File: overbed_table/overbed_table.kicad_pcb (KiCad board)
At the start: 2 copper layers, 10 parts, among them U1 TPS562201DDCR, U2 TPS562201DDCR, U3 TM1638

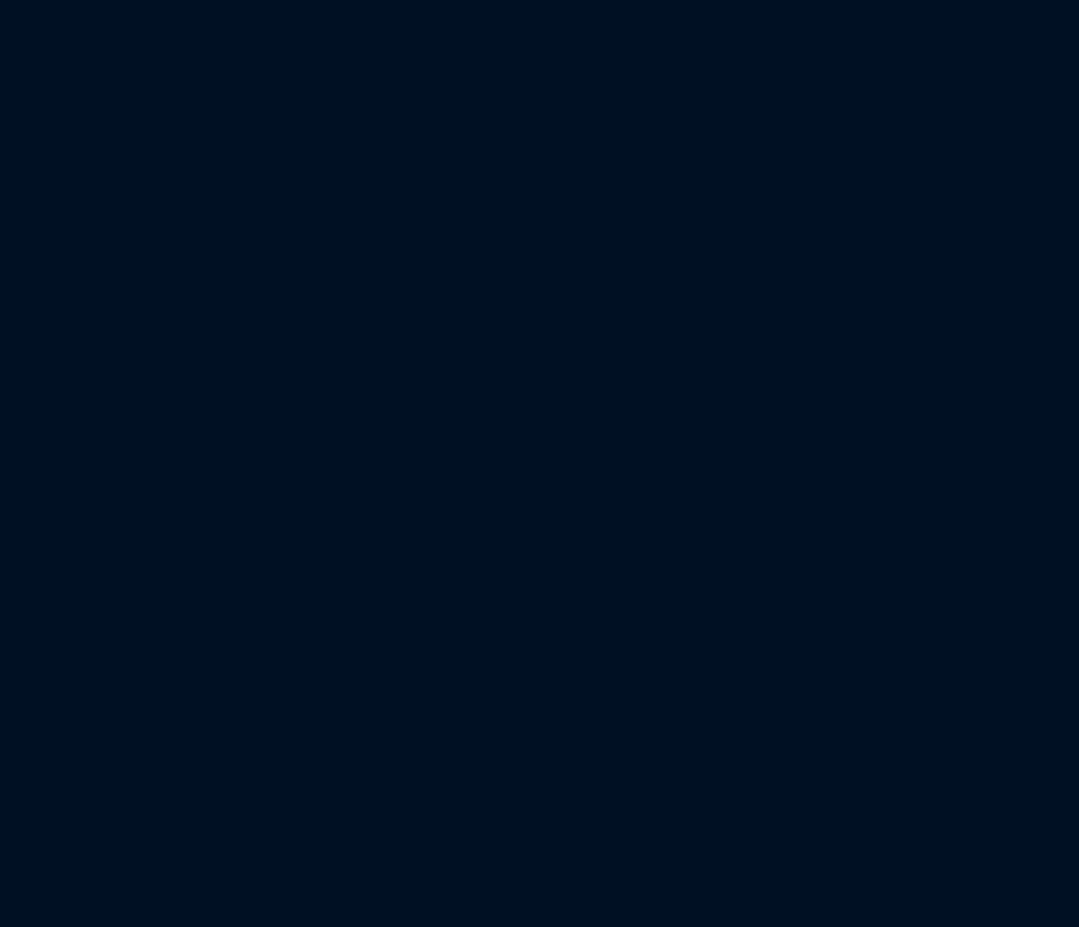
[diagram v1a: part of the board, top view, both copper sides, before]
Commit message: 更新步进驱动等
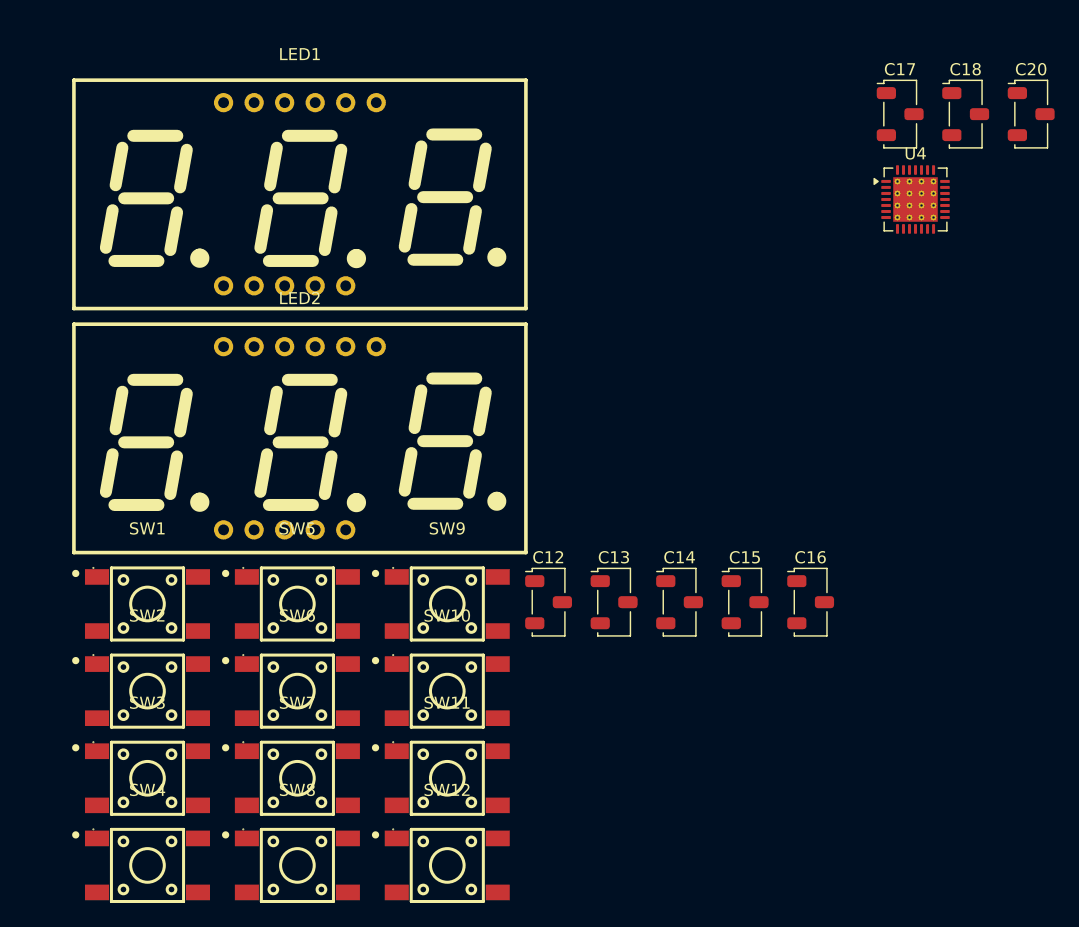
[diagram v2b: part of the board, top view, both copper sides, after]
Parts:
- added C12: 0.1uF, Button_Switch_SMD:Nidec_Copal_CAS-120A, F.Cu at (248.6, 111.6)
- added C13: 100uF, Button_Switch_SMD:Nidec_Copal_CAS-120A, F.Cu at (254.1, 111.6)
- added C14: 100pF, Button_Switch_SMD:Nidec_Copal_CAS-120A, F.Cu at (259.5, 111.6)
- added C15: 100pF, Button_Switch_SMD:Nidec_Copal_CAS-120A, F.Cu at (265.0, 111.6)
- added C16: 100pF, Button_Switch_SMD:Nidec_Copal_CAS-120A, F.Cu at (270.4, 111.6)
- added C17: 22nF, Button_Switch_SMD:Nidec_Copal_CAS-120A, F.Cu at (277.9, 71.0)
- added C18: 100nF, Button_Switch_SMD:Nidec_Copal_CAS-120A, F.Cu at (283.3, 71.0)
- added C20: 100nF, Button_Switch_SMD:Nidec_Copal_CAS-120A, F.Cu at (288.8, 71.0)
- added LED1: FJ5361BW, lcsc_footprints:C2938342_LED-SEG-TH_11P-L37_5-W19_0-P2_54-LS15_2-BL, F.Cu at (227.9, 77.6)
- added LED2: FJ5361BW, lcsc_footprints:C2938342_LED-SEG-TH_11P-L37_5-W19_0-P2_54-LS15_2-BL, F.Cu at (227.9, 97.9)
- added SW1: KH-6X6X6H-STM, lcsc_footprints:C2837532_SW-SMD_4P-L6_0-W6_0-P4_50-LS9_0_KH-6X6X6H-STM, F.Cu at (215.3, 111.7)
- added SW10: KH-6X6X6H-STM, lcsc_footprints:C2837532_SW-SMD_4P-L6_0-W6_0-P4_50-LS9_0_KH-6X6X6H-STM, F.Cu at (240.2, 119.0)
- added SW11: KH-6X6X6H-STM, lcsc_footprints:C2837532_SW-SMD_4P-L6_0-W6_0-P4_50-LS9_0_KH-6X6X6H-STM, F.Cu at (240.2, 126.2)
- added SW12: KH-6X6X6H-STM, lcsc_footprints:C2837532_SW-SMD_4P-L6_0-W6_0-P4_50-LS9_0_KH-6X6X6H-STM, F.Cu at (240.2, 133.5)
- added SW2: KH-6X6X6H-STM, lcsc_footprints:C2837532_SW-SMD_4P-L6_0-W6_0-P4_50-LS9_0_KH-6X6X6H-STM, F.Cu at (215.3, 119.0)
- added SW3: KH-6X6X6H-STM, lcsc_footprints:C2837532_SW-SMD_4P-L6_0-W6_0-P4_50-LS9_0_KH-6X6X6H-STM, F.Cu at (215.3, 126.2)
- added SW4: KH-6X6X6H-STM, lcsc_footprints:C2837532_SW-SMD_4P-L6_0-W6_0-P4_50-LS9_0_KH-6X6X6H-STM, F.Cu at (215.3, 133.5)
- added SW5: KH-6X6X6H-STM, lcsc_footprints:C2837532_SW-SMD_4P-L6_0-W6_0-P4_50-LS9_0_KH-6X6X6H-STM, F.Cu at (227.7, 111.7)
- added SW6: KH-6X6X6H-STM, lcsc_footprints:C2837532_SW-SMD_4P-L6_0-W6_0-P4_50-LS9_0_KH-6X6X6H-STM, F.Cu at (227.7, 119.0)
- added SW7: KH-6X6X6H-STM, lcsc_footprints:C2837532_SW-SMD_4P-L6_0-W6_0-P4_50-LS9_0_KH-6X6X6H-STM, F.Cu at (227.7, 126.2)
- added SW8: KH-6X6X6H-STM, lcsc_footprints:C2837532_SW-SMD_4P-L6_0-W6_0-P4_50-LS9_0_KH-6X6X6H-STM, F.Cu at (227.7, 133.5)
- added SW9: KH-6X6X6H-STM, lcsc_footprints:C2837532_SW-SMD_4P-L6_0-W6_0-P4_50-LS9_0_KH-6X6X6H-STM, F.Cu at (240.2, 111.7)
- added U4: TMC2209-LA, Package_DFN_QFN:VQFN-28-1EP_5x5mm_P0.5mm_EP3.7x3.7mm_ThermalVias, F.Cu at (279.2, 78.1)
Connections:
- U3 pad 10: unconnected-(U3-SEG6/K6-Pad10) -> /数码管_按钮/SEG6
- U3 pad 11: unconnected-(U3-SEG7/K7-Pad11) -> /数码管_按钮/SEG7
- U3 pad 12: unconnected-(U3-SEG8/K8-Pad12) -> /数码管_按钮/SEG8
- U3 pad 15: unconnected-(U3-VDD-Pad15) -> +5V
- U3 pad 18: unconnected-(U3-GND-Pad18) -> GND
- U3 pad 19: unconnected-(U3-GR6-Pad19) -> /数码管_按钮/GRID6
- U3 pad 2: unconnected-(U3-K2-Pad2) -> Net-(SW5-A)
- U3 pad 20: unconnected-(U3-GR5-Pad20) -> /数码管_按钮/GRID5
- U3 pad 21: unconnected-(U3-GR4-Pad21) -> /数码管_按钮/GRID4
- U3 pad 22: unconnected-(U3-GR3-Pad22) -> /数码管_按钮/GRID3
- U3 pad 23: unconnected-(U3-GR2-Pad23) -> /数码管_按钮/GRID2
- U3 pad 24: unconnected-(U3-GR1-Pad24) -> /数码管_按钮/GRID1
- U3 pad 25: unconnected-(U3-GND-Pad25) -> GND
- U3 pad 26: unconnected-(U3-DIO-Pad26) -> /数码管_按钮/DIO
- U3 pad 27: unconnected-(U3-CLK-Pad27) -> /数码管_按钮/CLK
- U3 pad 28: unconnected-(U3-STB-Pad28) -> /数码管_按钮/STB
- U3 pad 3: unconnected-(U3-K3-Pad3) -> Net-(SW1-A)
- U3 pad 4: unconnected-(U3-VDD-Pad4) -> +5V
- U3 pad 5: unconnected-(U3-SEG1/K1-Pad5) -> /数码管_按钮/SEG1
- U3 pad 6: unconnected-(U3-SEG2/K2-Pad6) -> /数码管_按钮/SEG2
- U3 pad 7: unconnected-(U3-SEG3/K3-Pad7) -> /数码管_按钮/SEG3
- U3 pad 8: unconnected-(U3-SEG4/K4-Pad8) -> /数码管_按钮/SEG4
- U3 pad 9: unconnected-(U3-SEG5/K5-Pad9) -> /数码管_按钮/SEG5

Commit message: 更新原理图
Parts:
- added C1: 10uF, Capacitor_SMD:C_0603_1608Metric, F.Cu at (78.6, 144.2)
- added C21: C, Display_7Segment:HDSP-7401, F.Cu at (46.5, 118.7)
- added C22: 100nF, Display_7Segment:HDSP-7401, F.Cu at (55.8, 118.7)
- added C23: 100nF, Display_7Segment:HDSP-7401, F.Cu at (65.1, 118.7)
- added C24: 100uF, Display_7Segment:HDSP-7401, F.Cu at (74.4, 118.7)
- added C25: 100nF, lcsc_footprints:C5342036_HVSSOP-28_L7_1-W3_0-P0_50-LS4_9-BL-EP, F.Cu at (33.8, 108.9)
- added C26: 220uF, lcsc_footprints:C5342036_HVSSOP-28_L7_1-W3_0-P0_50-LS4_9-BL-EP, F.Cu at (26.2, 119.1)
- added C27: 10nF, lcsc_footprints:C5342036_HVSSOP-28_L7_1-W3_0-P0_50-LS4_9-BL-EP, F.Cu at (24.8, 132.4)
- added C28: 100nF, lcsc_footprints:C5342036_HVSSOP-28_L7_1-W3_0-P0_50-LS4_9-BL-EP, F.Cu at (38.2, 134.1)
- added C29: 100nF, lcsc_footprints:C5342036_HVSSOP-28_L7_1-W3_0-P0_50-LS4_9-BL-EP, F.Cu at (21.2, 150.1)
- added C30: 100nF, lcsc_footprints:C5342036_HVSSOP-28_L7_1-W3_0-P0_50-LS4_9-BL-EP, F.Cu at (18.8, 167.1)
- added C31: 10uF, Capacitor_SMD:C_0603_1608Metric, F.Cu at (58.2, 147.3)
- added C31: 10uF, lcsc_footprints:C19188399_SOT-563-6_L1_6-W1_2-P0_50-LS1_6-BL, F.Cu at (57.8, 144.4)
- added C32: 10uF, Capacitor_SMD:C_0603_1608Metric, F.Cu at (58.2, 149.8)
- added C32: 10uF, lcsc_footprints:C19188399_SOT-563-6_L1_6-W1_2-P0_50-LS1_6-BL, F.Cu at (60.9, 144.4)
- added C33: 100nF, lcsc_footprints:C19188399_SOT-563-6_L1_6-W1_2-P0_50-LS1_6-BL, F.Cu at (64.0, 144.4)
- added C34: 22uF, lcsc_footprints:C19188399_SOT-563-6_L1_6-W1_2-P0_50-LS1_6-BL, F.Cu at (67.0, 144.4)
- added C35: 22uF, lcsc_footprints:C19188399_SOT-563-6_L1_6-W1_2-P0_50-LS1_6-BL, F.Cu at (70.1, 144.4)
- added C36: 22uF, lcsc_footprints:C19188399_SOT-563-6_L1_6-W1_2-P0_50-LS1_6-BL, F.Cu at (73.1, 144.4)
- added C4: 10uF, Capacitor_SMD:C_0603_1608Metric, F.Cu at (78.6, 146.7)
- added D1: 1N4148W, PCM_Diode_SMD_AKL:D_SOD-123, F.Cu at (47.3, 145.0)
- added D2: 1N4148W, PCM_Diode_SMD_AKL:D_SOD-123, F.Cu at (47.3, 149.1)
- added D3: 1N4148W, PCM_Diode_SMD_AKL:D_SOD-123, F.Cu at (47.3, 153.2)
- added D4: 1N4148W, PCM_Diode_SMD_AKL:D_SOD-123, F.Cu at (47.3, 157.3)
- added D5: 1N4148W, PCM_Diode_SMD_AKL:D_SOD-123, F.Cu at (47.3, 161.4)
- added D6: 1N4148W, PCM_Diode_SMD_AKL:D_SOD-123, F.Cu at (47.3, 165.5)
- added Q1: BSS138, PCM_Package_TO_SOT_SMD_AKL:SOT-23, F.Cu at (62.6, 160.4)
- added R10: 1k, PCM_SparkFun-Resistor:R_0603_1608Metric, F.Cu at (46.3, 132.2)
- added R11: 10k, PCM_SparkFun-Resistor:R_0603_1608Metric, F.Cu at (46.3, 134.7)
- added R12: 0.15, PCM_SparkFun-Resistor:R_0603_1608Metric, F.Cu at (46.3, 137.2)
- added R13: 0.15, PCM_SparkFun-Resistor:R_0603_1608Metric, F.Cu at (46.3, 139.7)
- added R14: 10k, PCM_SparkFun-Resistor:R_0603_1608Metric, F.Cu at (40.3, 117.8)
- added R15: 10k, PCM_SparkFun-Resistor:R_0603_1608Metric, F.Cu at (40.3, 120.3)
- added R16: 1k, PCM_SparkFun-Resistor:R_0603_1608Metric, F.Cu at (40.3, 122.8)
- added R17: 4.7k, PCM_SparkFun-Resistor:R_0603_1608Metric, F.Cu at (40.3, 125.3)
- added R18: 33.2k, PCM_SparkFun-Resistor:R_0603_1608Metric, F.Cu at (58.2, 152.3)
- added R19: 10k, PCM_SparkFun-Resistor:R_0603_1608Metric, F.Cu at (58.2, 154.8)
- added R3: 33.2k, PCM_SparkFun-Resistor:R_0603_1608Metric, F.Cu at (78.6, 149.2)
- added R4: 10k, PCM_SparkFun-Resistor:R_0603_1608Metric, F.Cu at (78.6, 151.7)
- added R5: 10k, PCM_SparkFun-Resistor:R_0603_1608Metric, F.Cu at (52.2, 144.2)
- added R6: 10k, PCM_SparkFun-Resistor:R_0603_1608Metric, F.Cu at (52.2, 146.7)
- added R7: 10k, PCM_SparkFun-Resistor:R_0603_1608Metric, F.Cu at (52.2, 149.2)
- added R8: 4.7k, PCM_SparkFun-Resistor:R_0603_1608Metric, F.Cu at (58.2, 159.3)
- added R9: 4.7k, PCM_SparkFun-Resistor:R_0603_1608Metric, F.Cu at (58.2, 161.8)
- added U5: DRV8243SQDGQRQ1, lcsc_footprints:C5342036_HVSSOP-28_L7_1-W3_0-P0_50-LS4_9-BL-EP, F.Cu at (36.8, 167.6)
- added U6: TPS562201DDCR, lcsc_footprints:C90061_SOT-23-6_L2_9-W1_6-P0_95-LS2_8-BR, F.Cu at (127.5, 139.0)

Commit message: 原理图V1.0
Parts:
- removed the C1 at (78.6, 144.2)
- removed the C1 at (103.1, 90.3)
- removed the C31 at (58.2, 147.3)
- removed the C31 at (57.8, 144.4)
- removed the C32 at (58.2, 149.8)
- removed the C32 at (60.9, 144.4)
- removed the C4 at (112.3, 90.3)
- removed the C4 at (78.6, 146.7)
- added C1: 1uF, Capacitor_SMD:C_0603_1608Metric, F.Cu at (93.5, 53.8)
- added C10: 100nF, Capacitor_SMD:C_0805_2012Metric, F.Cu at (166.3, 153.3)
- added C11: 22uF, Capacitor_SMD:C_0805_2012Metric, F.Cu at (166.3, 156.3)
- added C19: 100pF, Capacitor_SMD:C_0603_1608Metric, F.Cu at (98.4, 102.9)
- added C31: 100nF, Capacitor_SMD:C_0603_1608Metric, F.Cu at (173.9, 72.9)
- added C32: 4.7uF, Capacitor_SMD:C_0603_1608Metric, F.Cu at (173.9, 75.4)
- added C37: 4.7uF, Capacitor_SMD:C_0603_1608Metric, F.Cu at (181.9, 164.1)
- added C38: 10uF, Capacitor_SMD:C_0805_2012Metric, F.Cu at (128.4, 155.8)
- added C38: 10uF, Capacitor_SMD:C_0603_1608Metric, F.Cu at (132.6, 155.5)
- added C39: 10uF, Capacitor_SMD:C_0603_1608Metric, F.Cu at (132.6, 158.0)
- added C39: 10uF, Capacitor_SMD:C_0805_2012Metric, F.Cu at (128.4, 158.8)
- added C4: 1uF, Capacitor_SMD:C_0603_1608Metric, F.Cu at (93.5, 58.9)
- added C40: 100nF, Capacitor_SMD:C_0805_2012Metric, F.Cu at (128.4, 161.8)
- added C41: 22uF, Capacitor_SMD:C_0805_2012Metric, F.Cu at (128.4, 164.8)
- added C42: 22uF, Capacitor_SMD:C_0805_2012Metric, F.Cu at (128.4, 167.8)
- added C43: 22uF, Capacitor_SMD:C_0805_2012Metric, F.Cu at (128.4, 170.8)
- added C44: 1uF, Capacitor_SMD:C_0603_1608Metric, F.Cu at (147.5, 124.6)
- added C45: 1uF, Capacitor_SMD:C_0603_1608Metric, F.Cu at (147.5, 127.1)
- added C46: 100nF, Capacitor_SMD:C_0603_1608Metric, F.Cu at (147.5, 129.6)
- added C47: 1uF, Capacitor_SMD:C_0603_1608Metric, F.Cu at (147.5, 132.1)
- added C48: 1uF, Capacitor_SMD:C_0603_1608Metric, F.Cu at (147.5, 134.6)
- added C49: 1nF, Capacitor_SMD:C_0603_1608Metric, F.Cu at (151.5, 124.6)
- added C50: 1uF, Capacitor_SMD:C_0603_1608Metric, F.Cu at (151.5, 127.1)
- added C51: 1nF, Capacitor_SMD:C_0603_1608Metric, F.Cu at (151.5, 129.6)
- added C52: 1uF, Capacitor_SMD:C_0603_1608Metric, F.Cu at (155.3, 59.9)
- added C53: 1uF, Capacitor_SMD:C_0603_1608Metric, F.Cu at (155.3, 62.4)
- added C54: 100nF, Capacitor_SMD:C_0603_1608Metric, F.Cu at (155.3, 64.9)
- added C55: 1uF, Capacitor_SMD:C_0603_1608Metric, F.Cu at (155.3, 67.4)
- added C56: 1uF, Capacitor_SMD:C_0603_1608Metric, F.Cu at (155.3, 69.9)
- added C57: 1nF, Capacitor_SMD:C_0603_1608Metric, F.Cu at (159.3, 59.9)
- added C58: 1uF, Capacitor_SMD:C_0603_1608Metric, F.Cu at (159.3, 62.4)
- added C59: 1nF, Capacitor_SMD:C_0603_1608Metric, F.Cu at (159.3, 64.9)
- added C60: 100nF, Capacitor_SMD:C_0603_1608Metric, F.Cu at (173.9, 38.3)
- added C61: 100nF, Capacitor_SMD:C_0603_1608Metric, F.Cu at (173.9, 40.8)
- added C62: 100nF, Capacitor_SMD:C_0603_1608Metric, F.Cu at (173.9, 43.3)
- added C63: 100uF, Capacitor_SMD:CP_Elec_6.3x7.7, F.Cu at (181.1, 41.1)
- added C64: 100nF, Capacitor_SMD:C_0603_1608Metric, F.Cu at (173.9, 45.8)
- added C65: 100nF, Capacitor_SMD:C_0603_1608Metric, F.Cu at (173.9, 48.3)
- added C66: 4.7uF, Capacitor_SMD:C_0603_1608Metric, F.Cu at (173.9, 50.8)
- added C67: 22nF, Capacitor_SMD:C_0603_1608Metric, F.Cu at (173.9, 53.3)
- added C68: 100nF, Capacitor_SMD:C_0603_1608Metric, F.Cu at (181.9, 147.0)
- added C69: 4.7uF, Capacitor_SMD:C_0603_1608Metric, F.Cu at (181.9, 149.5)
- added C7: 1uF, Capacitor_SMD:C_0603_1608Metric, F.Cu at (97.5, 56.3)
- added C70: 10uF, Capacitor_SMD:C_0603_1608Metric, F.Cu at (116.8, 155.5)
- added C70: 10uF, Capacitor_SMD:C_0805_2012Metric, F.Cu at (112.5, 155.8)
- added C71: 10uF, Capacitor_SMD:C_0603_1608Metric, F.Cu at (116.8, 158.0)
- added C71: 10uF, Capacitor_SMD:C_0805_2012Metric, F.Cu at (112.5, 158.8)
- added C72: 100nF, Capacitor_SMD:C_0805_2012Metric, F.Cu at (112.5, 161.8)
- added C73: 22uF, Capacitor_SMD:C_0805_2012Metric, F.Cu at (112.5, 164.8)
- added C74: 22uF, Capacitor_SMD:C_0805_2012Metric, F.Cu at (112.5, 167.8)
- added C75: 22uF, Capacitor_SMD:C_0805_2012Metric, F.Cu at (112.5, 170.8)
- added C76: 100nF, Capacitor_SMD:C_0603_1608Metric, F.Cu at (172.2, 115.0)
- added C77: 470uF, Capacitor_SMD:CP_Elec_10x10.5, F.Cu at (171.4, 107.7)
- added C78: 100nF, Capacitor_SMD:C_0603_1608Metric, F.Cu at (120.1, 90.9)
- added C8: 10uF, Capacitor_SMD:C_0805_2012Metric, F.Cu at (166.3, 147.3)
- added C8: 10uF, Capacitor_SMD:C_0603_1608Metric, F.Cu at (170.5, 147.0)
- added C9: 10uF, Capacitor_SMD:C_0603_1608Metric, F.Cu at (170.5, 149.5)
- added C9: 10uF, Capacitor_SMD:C_0805_2012Metric, F.Cu at (166.3, 150.3)
- added CN10: DLL-5569-2AW, lcsc_footprints:C22365654_CONN-TH_DLL-5569-2AW-GOLD-GR, F.Cu at (112.4, 80.4)
- added CN2: KF2EDGRC-5.08-4P, lcsc_footprints:C441238_CONN-TH_4P-P5_08_KF2EDGRC-5_08-4P, F.Cu at (63.1, 65.5)
- added CN3: KF2EDGRC-5.08-4P, lcsc_footprints:C441238_CONN-TH_4P-P5_08_KF2EDGRC-5_08-4P, F.Cu at (63.1, 78.9)
- added CN4: DLL-5569-6AW, lcsc_footprints:C22365656_CONN-TH_6P-P4_20_C9900016025, F.Cu at (129.8, 106.3)
- added CN5: KF2EDGRC-5.08-4P, lcsc_footprints:C441238_CONN-TH_4P-P5_08_KF2EDGRC-5_08-4P, F.Cu at (133.9, 125.2)
- added CN6: DLL-5569-6AW, lcsc_footprints:C22365656_CONN-TH_6P-P4_20_C9900016025, F.Cu at (137.6, 41.6)
- added CN7: KF2EDGRC-5.08-4P, lcsc_footprints:C441238_CONN-TH_4P-P5_08_KF2EDGRC-5_08-4P, F.Cu at (141.7, 60.6)
- added CN8: DLL-5569-2AW, lcsc_footprints:C22365654_CONN-TH_DLL-5569-2AW-GOLD-GR, F.Cu at (99.1, 80.4)
- added CN9: DLL-5569-2AW, lcsc_footprints:C22365654_CONN-TH_DLL-5569-2AW-GOLD-GR, F.Cu at (105.7, 80.4)
- added D7: 1N4148W, PCM_Diode_SMD_AKL:D_SOD-123, F.Cu at (93.4, 120.1)
- added D8: 1N4148W, PCM_Diode_SMD_AKL:D_SOD-123, F.Cu at (93.4, 124.2)
- added F1: 3557-2, lcsc_footprints:C352820_FUSE-TH_4P-L19_8-W6_7_3557-2, F.Cu at (85.2, 67.5)
- added F2: 3557-2, lcsc_footprints:C352820_FUSE-TH_4P-L19_8-W6_7_3557-2, F.Cu at (85.2, 75.5)
- added F3: 3557-2, lcsc_footprints:C352820_FUSE-TH_4P-L19_8-W6_7_3557-2, F.Cu at (85.2, 83.5)
- added H1: LAIL-PZ2.54-4P-L, lcsc_footprints:C54950602_CONN-TH_LAIL-PZ2_54-4P-L, F.Cu at (66.0, 92.3)
- added H2: LAIL-PZ2.54-6P-L, lcsc_footprints:C54950607_CONN-TH_LAIL-PZ2_54-6P-L, F.Cu at (130.6, 147.8)
- added H3: LAIL-PZ2.54-6P-L, lcsc_footprints:C54950607_CONN-TH_LAIL-PZ2_54-6P-L, F.Cu at (138.4, 83.2)
- added L1: FXL0630-3R3-M, lcsc_footprints:C167219_IND-SMD_L7_0-W6_6, F.Cu at (173.2, 159.7)
- added L2: FXL0630-3R3-M, lcsc_footprints:C167219_IND-SMD_L7_0-W6_6, F.Cu at (151.2, 158.2)
- added L3: FXL0630-3R3-M, lcsc_footprints:C167219_IND-SMD_L7_0-W6_6, F.Cu at (135.3, 168.2)
- added L4: FXL0630-3R3-M, lcsc_footprints:C167219_IND-SMD_L7_0-W6_6, F.Cu at (119.5, 168.2)
- added Q2: BSS138, PCM_Package_TO_SOT_SMD_AKL:SOT-23, F.Cu at (187.0, 130.8)
- added Q3: BSS138, PCM_Package_TO_SOT_SMD_AKL:SOT-23, F.Cu at (187.0, 135.5)
- added Q4: AON7524, lcsc_footprints:C431195_DFN-8_L3_0-W3_0-P0_65-BL, F.Cu at (149.2, 92.0)
- added Q5: AON7524, lcsc_footprints:C431195_DFN-8_L3_0-W3_0-P0_65-BL, F.Cu at (182.8, 104.0)
- added Q6: AON7524, lcsc_footprints:C431195_DFN-8_L3_0-W3_0-P0_65-BL, F.Cu at (159.6, 92.0)
- added R2: 10k, PCM_SparkFun-Resistor:R_0603_1608Metric, F.Cu at (97.5, 61.4)
- added R20: 10k, PCM_SparkFun-Resistor:R_0603_1608Metric, F.Cu at (172.2, 139.5)
- added R21: 10k, PCM_SparkFun-Resistor:R_0603_1608Metric, F.Cu at (172.2, 142.0)
- added R22: 1k, PCM_SparkFun-Resistor:R_0603_1608Metric, F.Cu at (173.9, 80.4)
- added R23: 10k, PCM_SparkFun-Resistor:R_0603_1608Metric, F.Cu at (173.9, 82.9)
- added R24: 0.15, Resistor_SMD:R_1206_3216Metric, F.Cu at (183.0, 78.6)
- added R25: 0.15, Resistor_SMD:R_1206_3216Metric, F.Cu at (183.0, 82.0)
- added R26: 10k, PCM_SparkFun-Resistor:R_0603_1608Metric, F.Cu at (173.9, 89.9)
- added R27: 120, PCM_SparkFun-Resistor:R_0603_1608Metric, F.Cu at (173.9, 92.5)
- added R28: 390, PCM_SparkFun-Resistor:R_0603_1608Metric, F.Cu at (173.9, 95.0)
- added R29: 390, PCM_SparkFun-Resistor:R_0603_1608Metric, F.Cu at (173.9, 97.5)
- added R30: 10k, PCM_SparkFun-Resistor:R_0603_1608Metric, F.Cu at (134.6, 93.4)
- added R31: 120, PCM_SparkFun-Resistor:R_0603_1608Metric, F.Cu at (134.6, 95.9)
- added R32: 4.7k, PCM_SparkFun-Resistor:R_0603_1608Metric, F.Cu at (181.9, 166.6)
- added R33: 4.7k, PCM_SparkFun-Resistor:R_0603_1608Metric, F.Cu at (181.9, 169.1)
- added R34: 10k, PCM_SparkFun-Resistor:R_0603_1608Metric, F.Cu at (181.9, 171.6)
- added R35: 33, PCM_SparkFun-Resistor:R_0603_1608Metric, F.Cu at (153.3, 90.9)
- added R36: 10k, PCM_SparkFun-Resistor:R_0603_1608Metric, F.Cu at (153.3, 93.4)
- added R37: 33, PCM_SparkFun-Resistor:R_0603_1608Metric, F.Cu at (186.9, 102.9)
- added R38: 10k, PCM_SparkFun-Resistor:R_0603_1608Metric, F.Cu at (186.9, 105.4)
- added R39: 33.2k, PCM_SparkFun-Resistor:R_0603_1608Metric, F.Cu at (132.6, 160.5)
- added R40: 10k, PCM_SparkFun-Resistor:R_0603_1608Metric, F.Cu at (132.6, 163.1)
- added R41: 10k, PCM_SparkFun-Resistor:R_0603_1608Metric, F.Cu at (151.5, 132.1)
- added R42: 0, PCM_SparkFun-Resistor:R_0603_1608Metric, F.Cu at (151.5, 134.6)
- added R43: 10k, PCM_SparkFun-Resistor:R_0603_1608Metric, F.Cu at (155.5, 124.6)
- added R44: 10k, PCM_SparkFun-Resistor:R_0603_1608Metric, F.Cu at (155.5, 127.1)
- added R45: 100, PCM_SparkFun-Resistor:R_0603_1608Metric, F.Cu at (155.5, 129.6)
- added R46: 10k, PCM_SparkFun-Resistor:R_0603_1608Metric, F.Cu at (155.5, 132.1)
- added R47: 100, PCM_SparkFun-Resistor:R_0603_1608Metric, F.Cu at (155.5, 134.6)
- added R48: 10k, PCM_SparkFun-Resistor:R_0603_1608Metric, F.Cu at (159.5, 124.6)
- added R49: 10k, PCM_SparkFun-Resistor:R_0603_1608Metric, F.Cu at (159.5, 127.1)
- added R50: 10k, PCM_SparkFun-Resistor:R_0603_1608Metric, F.Cu at (159.5, 129.6)
- added R51: 100, PCM_SparkFun-Resistor:R_0603_1608Metric, F.Cu at (159.5, 132.1)
- added R52: 100, PCM_SparkFun-Resistor:R_0603_1608Metric, F.Cu at (159.5, 134.6)
- added R53: 10k, PCM_SparkFun-Resistor:R_0603_1608Metric, F.Cu at (159.3, 67.4)
- added R54: 0, PCM_SparkFun-Resistor:R_0603_1608Metric, F.Cu at (159.3, 69.9)
- added R55: 10k, PCM_SparkFun-Resistor:R_0603_1608Metric, F.Cu at (163.3, 59.9)
- added R56: 10k, PCM_SparkFun-Resistor:R_0603_1608Metric, F.Cu at (163.3, 62.4)
- added R57: 100, PCM_SparkFun-Resistor:R_0603_1608Metric, F.Cu at (163.3, 64.9)
- added R58: 10k, PCM_SparkFun-Resistor:R_0603_1608Metric, F.Cu at (163.3, 67.4)
- added R59: 100, PCM_SparkFun-Resistor:R_0603_1608Metric, F.Cu at (163.3, 69.9)
- added R60: 10k, PCM_SparkFun-Resistor:R_0603_1608Metric, F.Cu at (167.3, 59.9)
- added R61: 10k, PCM_SparkFun-Resistor:R_0603_1608Metric, F.Cu at (167.3, 62.4)
- added R62: 10k, PCM_SparkFun-Resistor:R_0603_1608Metric, F.Cu at (167.3, 64.9)
- added R63: 100, PCM_SparkFun-Resistor:R_0603_1608Metric, F.Cu at (167.3, 67.4)
- added R64: 100, PCM_SparkFun-Resistor:R_0603_1608Metric, F.Cu at (167.3, 69.9)
- added R65: 1k, PCM_SparkFun-Resistor:R_0603_1608Metric, F.Cu at (173.9, 55.8)
- added R66: 10k, PCM_SparkFun-Resistor:R_0603_1608Metric, F.Cu at (173.9, 58.3)
- added R67: 0.15, Resistor_SMD:R_1206_3216Metric, F.Cu at (183.0, 54.1)
- added R68: 0.15, Resistor_SMD:R_1206_3216Metric, F.Cu at (183.0, 57.4)
- added R69: 4.7k, PCM_SparkFun-Resistor:R_0603_1608Metric, F.Cu at (181.9, 152.0)
- added R70: 4.7k, PCM_SparkFun-Resistor:R_0603_1608Metric, F.Cu at (181.9, 154.5)
- added R71: 10k, PCM_SparkFun-Resistor:R_0603_1608Metric, F.Cu at (181.9, 157.0)
- added R72: 33.2k, PCM_SparkFun-Resistor:R_0603_1608Metric, F.Cu at (116.8, 160.5)
- added R73: 10k, PCM_SparkFun-Resistor:R_0603_1608Metric, F.Cu at (116.8, 163.1)
- added R74: 10k, PCM_SparkFun-Resistor:R_0603_1608Metric, F.Cu at (172.2, 117.5)
- added R75: 10k, PCM_SparkFun-Resistor:R_0603_1608Metric, F.Cu at (172.2, 120.0)
- added R76: 10k, PCM_SparkFun-Resistor:R_0603_1608Metric, F.Cu at (120.1, 93.4)
- added R77: 120, PCM_SparkFun-Resistor:R_0603_1608Metric, F.Cu at (120.1, 95.9)
- added R78: 33, PCM_SparkFun-Resistor:R_0603_1608Metric, F.Cu at (163.7, 90.9)
- added R79: 10k, PCM_SparkFun-Resistor:R_0603_1608Metric, F.Cu at (163.7, 93.4)
- added SW13: KH-6X6X6H-STM, lcsc_footprints:C2837532_SW-SMD_4P-L6_0-W6_0-P4_50-LS9_0_KH-6X6X6H-STM, F.Cu at (83.2, 160.5)
- added SW14: KH-6X6X6H-STM, lcsc_footprints:C2837532_SW-SMD_4P-L6_0-W6_0-P4_50-LS9_0_KH-6X6X6H-STM, F.Cu at (83.2, 167.8)
- added SW15: KH-6X6X6H-STM, lcsc_footprints:C2837532_SW-SMD_4P-L6_0-W6_0-P4_50-LS9_0_KH-6X6X6H-STM, F.Cu at (156.3, 105.3)
- added SW16: KH-6X6X6H-STM, lcsc_footprints:C2837532_SW-SMD_4P-L6_0-W6_0-P4_50-LS9_0_KH-6X6X6H-STM, F.Cu at (156.3, 112.5)
- added SW17: KH-6X6X6H-STM, lcsc_footprints:C2837532_SW-SMD_4P-L6_0-W6_0-P4_50-LS9_0_KH-6X6X6H-STM, F.Cu at (164.2, 40.6)
- added SW18: KH-6X6X6H-STM, lcsc_footprints:C2837532_SW-SMD_4P-L6_0-W6_0-P4_50-LS9_0_KH-6X6X6H-STM, F.Cu at (164.2, 47.9)
- added TP1: TestPoint, PCM_SparkFun-Connector:TestPoint-1.0mm, F.Cu at (177.0, 70.8)
- added TP10: TestPoint, PCM_SparkFun-Connector:TestPoint-1.0mm, F.Cu at (179.1, 79.6)
- added TP11: 1.0mm, PCM_SparkFun-Connector:TestPoint-1.0mm, F.Cu at (185.0, 165.6)
- added TP12: 1.0mm, PCM_SparkFun-Connector:TestPoint-1.0mm, F.Cu at (185.0, 167.8)
- added TP13: 1.0mm, PCM_SparkFun-Connector:TestPoint-1.0mm, F.Cu at (185.0, 170.0)
- added TP14: 1.0mm, PCM_SparkFun-Connector:TestPoint-1.0mm, F.Cu at (154.7, 137.8)
- added TP15: 1.0mm, PCM_SparkFun-Connector:TestPoint-1.0mm, F.Cu at (154.7, 140.0)
- added TP16: 1.0mm, PCM_SparkFun-Connector:TestPoint-1.0mm, F.Cu at (154.7, 142.2)
- added TP17: 1.0mm, PCM_SparkFun-Connector:TestPoint-1.0mm, F.Cu at (154.7, 144.4)
- added TP18: 1.0mm, PCM_SparkFun-Connector:TestPoint-1.0mm, F.Cu at (162.5, 73.2)
- added TP19: 1.0mm, PCM_SparkFun-Connector:TestPoint-1.0mm, F.Cu at (162.5, 75.4)
- added TP2: TestPoint, PCM_SparkFun-Connector:TestPoint-1.0mm, F.Cu at (177.0, 73.0)
- added TP20: 1.0mm, PCM_SparkFun-Connector:TestPoint-1.0mm, F.Cu at (162.5, 77.6)
- added TP21: 1.0mm, PCM_SparkFun-Connector:TestPoint-1.0mm, F.Cu at (162.5, 79.7)
- added TP22: TestPoint, PCM_SparkFun-Connector:TestPoint-1.0mm, F.Cu at (177.0, 46.2)
- added TP23: TestPoint, PCM_SparkFun-Connector:TestPoint-1.0mm, F.Cu at (177.0, 48.4)
- added TP24: TestPoint, PCM_SparkFun-Connector:TestPoint-1.0mm, F.Cu at (177.0, 50.6)
- added TP25: TestPoint, PCM_SparkFun-Connector:TestPoint-1.0mm, F.Cu at (177.0, 52.8)
- added TP26: TestPoint, PCM_SparkFun-Connector:TestPoint-1.0mm, F.Cu at (177.0, 55.0)
- added TP27: TestPoint, PCM_SparkFun-Connector:TestPoint-1.0mm, F.Cu at (179.1, 46.2)
- added TP28: TestPoint, PCM_SparkFun-Connector:TestPoint-1.0mm, F.Cu at (179.1, 48.4)
- added TP29: TestPoint, PCM_SparkFun-Connector:TestPoint-1.0mm, F.Cu at (179.1, 50.6)
- added TP3: TestPoint, PCM_SparkFun-Connector:TestPoint-1.0mm, F.Cu at (177.0, 75.2)
- added TP30: TestPoint, PCM_SparkFun-Connector:TestPoint-1.0mm, F.Cu at (179.1, 52.8)
- added TP31: TestPoint, PCM_SparkFun-Connector:TestPoint-1.0mm, F.Cu at (179.1, 55.0)
- added TP32: 1.0mm, PCM_SparkFun-Connector:TestPoint-1.0mm, F.Cu at (185.0, 151.1)
- added TP33: 1.0mm, PCM_SparkFun-Connector:TestPoint-1.0mm, F.Cu at (185.0, 153.2)
- added TP34: 1.0mm, PCM_SparkFun-Connector:TestPoint-1.0mm, F.Cu at (185.0, 155.4)
- added TP4: TestPoint, PCM_SparkFun-Connector:TestPoint-1.0mm, F.Cu at (177.0, 77.4)
- added TP5: TestPoint, PCM_SparkFun-Connector:TestPoint-1.0mm, F.Cu at (177.0, 79.6)
- added TP6: TestPoint, PCM_SparkFun-Connector:TestPoint-1.0mm, F.Cu at (179.1, 70.8)
- added TP7: TestPoint, PCM_SparkFun-Connector:TestPoint-1.0mm, F.Cu at (179.1, 73.0)
- added TP8: TestPoint, PCM_SparkFun-Connector:TestPoint-1.0mm, F.Cu at (179.1, 75.2)
- added TP9: TestPoint, PCM_SparkFun-Connector:TestPoint-1.0mm, F.Cu at (179.1, 77.4)
- added U10: TPS562201DDCR, lcsc_footprints:C90061_SOT-23-6_L2_9-W1_6-P0_95-LS2_8-BR, F.Cu at (174.9, 147.9)
- added U11: TPS562201DDCR, lcsc_footprints:C90061_SOT-23-6_L2_9-W1_6-P0_95-LS2_8-BR, F.Cu at (152.9, 164.3)
- added U12: TM1638, lcsc_footprints:C19187_SOIC-28_L17_9-W7_5-P1_27-LS10_3-BL, F.Cu at (98.7, 148.9)
- added U13: SS6285M-SO-TP, lcsc_footprints:C5370898_SOIC-8_L4_9-W3_9-P1_27-LS6_0-BL, F.Cu at (167.1, 139.8)
- added U14: TMC2209-LA, Package_DFN_QFN:VQFN-28-1EP_5x5mm_P0.5mm_EP3.7x3.7mm_ThermalVias, F.Cu at (184.2, 73.4)
- added U15: SP3485EN, Package_SO:SOIC-8_3.9x4.9mm_P1.27mm, F.Cu at (180.1, 89.5)
- added U16: SP3485EN, Package_SO:SOIC-8_3.9x4.9mm_P1.27mm, F.Cu at (140.8, 93.0)
- added U17: VL53L0CXV0DH1, Sensor_Distance:ST_VL53L1x, F.Cu at (187.3, 162.5)
- added U18: TPS562201DDCR, lcsc_footprints:C90061_SOT-23-6_L2_9-W1_6-P0_95-LS2_8-BR, F.Cu at (137.0, 156.4)
- added U19: PY32F030K28U6TR, lcsc_footprints:C3018718_QFN-32_L5_0-W5_0-P0_50-TL-EP3_5, F.Cu at (157.4, 148.9)
- added U20: WAFER-XH254WZ-2A, lcsc_footprints:C7432691_CONN-TH_2P-P2_50_WAFER-XH254WZ-2A, F.Cu at (126.7, 138.0)
- added U21: WAFER-XH254WZ-2A, lcsc_footprints:C7432691_CONN-TH_2P-P2_50_WAFER-XH254WZ-2A, F.Cu at (135.4, 138.0)
- added U22: WAFER-XH254WZ-4A, lcsc_footprints:C7432693_CONN-TH_4P-P2_50_WAFER-XH254WZ-4A, F.Cu at (146.7, 138.0)
- added U23: KF128-5.08-2P, lcsc_footprints:C474952_CONN-TH_P5_08_KF128-5_08-2P, F.Cu at (116.0, 107.7)
- added U24: KF128-5.08-2P, lcsc_footprints:C474952_CONN-TH_P5_08_KF128-5_08-2P, F.Cu at (116.0, 119.6)
- added U25: PY32F030K28U6TR, lcsc_footprints:C3018718_QFN-32_L5_0-W5_0-P0_50-TL-EP3_5, F.Cu at (165.2, 84.2)
- added U26: WAFER-XH254WZ-2A, lcsc_footprints:C7432691_CONN-TH_2P-P2_50_WAFER-XH254WZ-2A, F.Cu at (134.5, 73.4)
- added U27: WAFER-XH254WZ-2A, lcsc_footprints:C7432691_CONN-TH_2P-P2_50_WAFER-XH254WZ-2A, F.Cu at (143.3, 73.4)
- added U28: WAFER-XH254WZ-4A, lcsc_footprints:C7432693_CONN-TH_4P-P2_50_WAFER-XH254WZ-4A, F.Cu at (154.5, 73.4)
- added U29: KF128-5.08-2P, lcsc_footprints:C474952_CONN-TH_P5_08_KF128-5_08-2P, F.Cu at (123.8, 43.0)
- added U30: KF128-5.08-2P, lcsc_footprints:C474952_CONN-TH_P5_08_KF128-5_08-2P, F.Cu at (123.8, 55.0)
- added U31: TMC2209-LA, Package_DFN_QFN:VQFN-28-1EP_5x5mm_P0.5mm_EP3.7x3.7mm_ThermalVias, F.Cu at (184.2, 48.8)
- added U32: VL53L0CXV0DH1, Sensor_Distance:ST_VL53L1x, F.Cu at (187.3, 147.9)
- added U33: TPS562201DDCR, lcsc_footprints:C90061_SOT-23-6_L2_9-W1_6-P0_95-LS2_8-BR, F.Cu at (121.2, 156.4)
- added U34: SS6285M-SO-TP, lcsc_footprints:C5370898_SOIC-8_L4_9-W3_9-P1_27-LS6_0-BL, F.Cu at (167.1, 117.7)
- added U35: SP3485EN, Package_SO:SOIC-8_3.9x4.9mm_P1.27mm, F.Cu at (126.4, 93.0)
- added U7: KF7620-7.62-2P, lcsc_footprints:C475104_CONN-TH_P7_62_KF7620-7_62-2P, F.Cu at (104.7, 90.8)
- added X1: AFA01-S05FCA-00, lcsc_footprints:C262753_FPC-SMD_AFA01-S05FCA-00, F.Cu at (97.5, 39.7)
- added X2: AFA01-S05FCA-00, lcsc_footprints:C262753_FPC-SMD_AFA01-S05FCA-00, F.Cu at (97.5, 47.5)
- added X3: AFA01-S05FCA-00, lcsc_footprints:C262753_FPC-SMD_AFA01-S05FCA-00, F.Cu at (143.4, 104.3)
- added X4: AFA01-S05FCA-00, lcsc_footprints:C262753_FPC-SMD_AFA01-S05FCA-00, F.Cu at (143.4, 112.1)
- added X5: AFA01-S05FCA-00, lcsc_footprints:C262753_FPC-SMD_AFA01-S05FCA-00, F.Cu at (151.3, 39.7)
- added X6: AFA01-S05FCA-00, lcsc_footprints:C262753_FPC-SMD_AFA01-S05FCA-00, F.Cu at (151.3, 47.5)
- C12: value 0.1uF -> 22uF; footprint Button_Switch_SMD:Nidec_Copal_CAS-120A -> Capacitor_SMD:C_0805_2012Metric
- C13: value 100uF -> 22uF; footprint Button_Switch_SMD:Nidec_Copal_CAS-120A -> Capacitor_SMD:C_0805_2012Metric
- C14, C15: value 100pF -> 10uF; footprint Button_Switch_SMD:Nidec_Copal_CAS-120A -> Capacitor_SMD:C_0805_2012Metric
- C16: value 100pF -> 100nF; footprint Button_Switch_SMD:Nidec_Copal_CAS-120A -> Capacitor_SMD:C_0805_2012Metric
- C17: value 22nF -> 22uF; footprint Button_Switch_SMD:Nidec_Copal_CAS-120A -> Capacitor_SMD:C_0805_2012Metric
- C18: value 100nF -> 22uF; footprint Button_Switch_SMD:Nidec_Copal_CAS-120A -> Capacitor_SMD:C_0805_2012Metric
- C2: value 22uF -> 470uF; footprint lcsc_footprints:C19188399_SOT-563-6_L1_6-W1_2-P0_50-LS1_6-BL -> Capacitor_SMD:CP_Elec_10x10.5
- C20: value 100nF -> 100pF; footprint Button_Switch_SMD:Nidec_Copal_CAS-120A -> Capacitor_SMD:C_0603_1608Metric
- C21: value C -> 100pF; footprint Display_7Segment:HDSP-7401 -> Capacitor_SMD:C_0603_1608Metric
- C22: value 100nF -> 100uF; footprint Display_7Segment:HDSP-7401 -> Capacitor_SMD:CP_Elec_6.3x7.7
- C23: value 100nF -> 0.1uF; footprint Display_7Segment:HDSP-7401 -> Capacitor_SMD:C_0603_1608Metric
- C24: value 100uF -> 100nF; footprint Display_7Segment:HDSP-7401 -> Capacitor_SMD:C_0603_1608Metric
- C25: value 100nF -> 470uF; footprint lcsc_footprints:C5342036_HVSSOP-28_L7_1-W3_0-P0_50-LS4_9-BL-EP -> Capacitor_SMD:CP_Elec_10x10.5
- C26: value 220uF -> 100nF; footprint lcsc_footprints:C5342036_HVSSOP-28_L7_1-W3_0-P0_50-LS4_9-BL-EP -> Capacitor_SMD:C_0603_1608Metric
- C27: value 10nF -> 100nF; footprint lcsc_footprints:C5342036_HVSSOP-28_L7_1-W3_0-P0_50-LS4_9-BL-EP -> Capacitor_SMD:C_0603_1608Metric
- C28, C30: footprint lcsc_footprints:C5342036_HVSSOP-28_L7_1-W3_0-P0_50-LS4_9-BL-EP -> Capacitor_SMD:C_0603_1608Metric
- C29: value 100nF -> 100uF; footprint lcsc_footprints:C5342036_HVSSOP-28_L7_1-W3_0-P0_50-LS4_9-BL-EP -> Capacitor_SMD:CP_Elec_6.3x7.7
- C3: value 100nF -> 1uF; footprint lcsc_footprints:C19188399_SOT-563-6_L1_6-W1_2-P0_50-LS1_6-BL -> Capacitor_SMD:C_0603_1608Metric
- C33: value 100nF -> 22nF; footprint lcsc_footprints:C19188399_SOT-563-6_L1_6-W1_2-P0_50-LS1_6-BL -> Capacitor_SMD:C_0603_1608Metric
- C34, C35, C36, C5: value 22uF -> 100nF; footprint lcsc_footprints:C19188399_SOT-563-6_L1_6-W1_2-P0_50-LS1_6-BL -> Capacitor_SMD:C_0603_1608Metric
- C6: value 22uF -> 10uF; footprint lcsc_footprints:C19188399_SOT-563-6_L1_6-W1_2-P0_50-LS1_6-BL -> Capacitor_SMD:C_0603_1608Metric
- D1: value 1N4148W -> SMCJ12A; footprint PCM_Diode_SMD_AKL:D_SOD-123 -> PCM_Diode_SMD_AKL:D_SMC
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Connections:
- C12 pad 1: +5V -> /+3V3
- C12 pad 2: GND -> /GND
- C13 pad 1: +5V -> /+3V3
- C13 pad 2: GND -> /GND
- C14 pad 1: /数码管_按钮/STB -> /+12V
- C14 pad 2: GND -> /GND
- C15 pad 1: /数码管_按钮/CLK -> /+12V
- C15 pad 2: GND -> /GND
- C16 pad 1: /数码管_按钮/DIO -> Net-(U11-VBST)
- C16 pad 2: GND -> Net-(U11-SW)
- C17 pad 1: Net-(U4-CPI) -> /12V_5V/5V_OUT
- C17 pad 2: Net-(U4-CPO) -> /GND
- C18 pad 1: Net-(U4-VCP) -> /12V_5V/5V_OUT
- C18 pad 2: +12V -> /GND
- C2 pad 1: /12V_3V3/3V3_OUT -> /+12V
- C2 pad 2: GND -> /GND
- C20 pad 1: +3V3 -> /数码管_按钮/CLK
- C20 pad 2: GND -> /数码管_按钮/GND_IN
- C21 pad 1: +3V3 -> /数码管_按钮/DIO
- C21 pad 2: GND -> /数码管_按钮/GND_IN
- C22 pad 1: +12V -> /数码管_按钮/5V_IN
- C22 pad 2: GND -> /数码管_按钮/GND_IN
- C23 pad 1: +12V -> /数码管_按钮/5V_IN
- C23 pad 2: GND -> /数码管_按钮/GND_IN
- C24 pad 1: +12V -> /桌脚小板_1/+12V
- C24 pad 2: GND -> /桌脚小板_1/GND
- C25 pad 1: +12V -> /桌脚小板_1/+12V
- C25 pad 2: GND -> /桌脚小板_1/GND
- C26 pad 1: +12V -> /桌脚小板_1/+3V3
- C26 pad 2: GND -> /桌脚小板_1/GND
- C27 pad 1: GND -> /桌脚小板_1/+12V
- C27 pad 2: /升降电机驱动/IPROPI -> /桌脚小板_1/GND
- C28 pad 1: /升降电机驱动/OUT1 -> /桌脚小板_1/+12V
- C28 pad 2: /升降电机驱动/OUT2 -> /桌脚小板_1/GND
- C29 pad 1: GND -> /桌脚小板_1/+12V
- C29 pad 2: /升降电机驱动/OUT1 -> /桌脚小板_1/GND
- C3 pad 1: Net-(U1-VBST) -> /GND
- C3 pad 2: Net-(U1-SW) -> Net-(U1-EN)
- C30 pad 1: GND -> /桌脚小板_1/+3V3
- C30 pad 2: /升降电机驱动/OUT2 -> /桌脚小板_1/GND
- C33 pad 1: Net-(U6-VBST) -> Net-(U14-CPI)
- C33 pad 2: Net-(U6-SW) -> Net-(U14-CPO)
- C34 pad 1: /12V_3V4/3V3_OUT -> /+3V3
- C34 pad 2: GND -> /GND
- C35 pad 1: /12V_3V4/3V3_OUT -> /桌脚小板_1/+3V3
- C35 pad 2: GND -> /桌脚小板_1/GND
- C36 pad 1: /12V_3V4/3V3_OUT -> /桌脚小板_1/TOF/+3V3
- C36 pad 2: GND -> /桌脚小板_1/TOF/GND
- C5 pad 1: /12V_3V3/3V3_OUT -> /GND
- C5 pad 2: GND -> /+3V3
- C6 pad 1: /12V_3V3/3V3_OUT -> /GND
- C6 pad 2: GND -> /+3V3
- D1 pad 1: Net-(D1-K) -> /+12V
- D1 pad 2: /数码管_按钮/SEG1 -> /GND
- D2 pad 1: Net-(D2-K) -> /+3V3
- D2 pad 2: /数码管_按钮/SEG2 -> Net-(D2-A)
- D3 pad 2: /数码管_按钮/SEG3 -> /数码管_按钮/SEG1
- D4 pad 2: /数码管_按钮/SEG4 -> /数码管_按钮/SEG2
- D5 pad 2: /数码管_按钮/SEG5 -> /数码管_按钮/SEG3
- D6 pad 2: /数码管_按钮/SEG6 -> /数码管_按钮/SEG4
- Q1 pad 1: /3V3_5V_转换器/3V3_IN -> /+3V3
- Q1 pad 2: /3V3_5V_转换器/3V3_SIG -> /3V3_5V_转换器/3V3_SIG0
- Q1 pad 3: /3V3_5V_转换器/5V_SIG -> /3V3_5V_转换器/5V_SIG0
- R1 pad 1: /12V_5V/5V_OUT -> /+3V3
- R1 pad 2: Net-(U2-VFB) -> /ESP32_EN
- R10 pad 1: /步进驱动/UART_RX -> Net-(U11-VFB)
- R10 pad 2: /步进驱动/UART_TX -> /GND
- R11 pad 1: /步进驱动/EN -> /数码管_按钮/STB
- R11 pad 2: +3V3 -> /数码管_按钮/5V_IN
- R12 pad 1: Net-(U4-BRB) -> /数码管_按钮/CLK
- R12 pad 2: GND -> /数码管_按钮/5V_IN
- R13 pad 1: Net-(U4-BRA) -> /数码管_按钮/DIO
- R13 pad 2: GND -> /数码管_按钮/5V_IN
- R14 pad 1: +3V3 -> /+3V3
- R14 pad 2: /升降电机驱动/DRVOFF -> /3V3_5V_转换器/3V3_SIG0
- R15 pad 1: +3V3 -> /+3V3
- R15 pad 2: /升降电机驱动/nSLEEP -> /3V3_5V_转换器/3V3_SIG1
- R16 pad 1: GND -> /+3V3
- R16 pad 2: /升降电机驱动/IPROPI -> /3V3_5V_转换器/3V3_SIG2
- R17 pad 1: +3V3 -> /12V_5V/5V_OUT
- R17 pad 2: /升降电机驱动/nFAULT -> /3V3_5V_转换器/5V_SIG0
- R18 pad 1: Net-(U6-VFB) -> /12V_5V/5V_OUT
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
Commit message: 更新原理图
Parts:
- removed the C38 at (128.4, 155.8)
- removed the C38 at (132.6, 155.5)
- removed the C39 at (132.6, 158.0)
- removed the C39 at (128.4, 158.8)
- removed the C70 at (116.8, 155.5)
- removed the C70 at (112.5, 155.8)
- removed the C71 at (116.8, 158.0)
- removed the C71 at (112.5, 158.8)
- removed the C8 at (166.3, 147.3)
- removed the C8 at (170.5, 147.0)
- removed the C9 at (170.5, 149.5)
- removed the C9 at (166.3, 150.3)
- added C38: 10uF, Capacitor_SMD:C_0603_1608Metric, F.Cu at (170.6, 157.5)
- added C38: 10uF, Capacitor_SMD:C_0805_2012Metric, F.Cu at (166.4, 157.8)
- added C39: 10uF, Capacitor_SMD:C_0805_2012Metric, F.Cu at (166.4, 160.8)
- added C39: 10uF, Capacitor_SMD:C_0603_1608Metric, F.Cu at (170.6, 160.0)
- added C70: 10uF, Capacitor_SMD:C_0603_1608Metric, F.Cu at (154.8, 157.5)
- added C70: 10uF, Capacitor_SMD:C_0805_2012Metric, F.Cu at (150.5, 157.8)
- added C71: 10uF, Capacitor_SMD:C_0603_1608Metric, F.Cu at (154.8, 160.0)
- added C71: 10uF, Capacitor_SMD:C_0805_2012Metric, F.Cu at (150.5, 160.8)
- added C8: 10uF, Capacitor_SMD:C_0603_1608Metric, F.Cu at (208.5, 149.0)
- added C8: 10uF, Capacitor_SMD:C_0805_2012Metric, F.Cu at (204.3, 149.3)
- added C9: 10uF, Capacitor_SMD:C_0805_2012Metric, F.Cu at (204.3, 152.3)
- added C9: 10uF, Capacitor_SMD:C_0603_1608Metric, F.Cu at (208.5, 151.5)
- moved CN10 38.1 mm to (150.4, 82.4)
- moved D1 38.1 mm to (147.2, 58.0)
- moved U1 38.1 mm to (100.8, 98.6)
- moved C1 38.1 mm to (131.5, 55.8)
- moved C10 38.1 mm to (204.3, 155.3)
- moved C11 38.1 mm to (204.3, 158.3)
- moved C12 38.1 mm to (204.3, 161.3)
- moved C13 38.1 mm to (204.3, 164.3)
- moved C14 38.1 mm to (182.2, 157.8)
- moved C15 38.1 mm to (182.2, 160.8)
- moved C16 38.1 mm to (182.2, 163.8)
- moved C17 38.1 mm to (182.2, 166.8)
- moved C18 38.1 mm to (182.2, 169.8)
- moved C19 38.1 mm to (136.4, 104.9)
- moved C2 38.1 mm to (120.1, 95.5)
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
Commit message: 更新pcb
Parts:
- removed the C38 at (170.6, 157.5)
- removed the C38 at (166.4, 157.8)
- removed the C39 at (166.4, 160.8)
- removed the C39 at (170.6, 160.0)
- removed the C70 at (154.8, 157.5)
- removed the C70 at (150.5, 157.8)
- removed the C71 at (154.8, 160.0)
- removed the C71 at (150.5, 160.8)
- removed the C8 at (208.5, 149.0)
- removed the C8 at (204.3, 149.3)
- removed the C9 at (204.3, 152.3)
- removed the C9 at (208.5, 151.5)
- added C38: 10uF, Capacitor_SMD:C_0805_2012Metric, F.Cu at (256.3, 25.5)
- added C39: 10uF, Capacitor_SMD:C_0805_2012Metric, F.Cu at (256.3, 28.5)
- added C70: 10uF, Capacitor_SMD:C_0805_2012Metric, F.Cu at (251.5, 130.7)
- added C71: 10uF, Capacitor_SMD:C_0805_2012Metric, F.Cu at (251.5, 133.8)
- added C8: 10uF, Capacitor_SMD:C_0805_2012Metric, F.Cu at (58.6, 44.1)
- added C9: 10uF, Capacitor_SMD:C_0805_2012Metric, F.Cu at (60.6, 44.1)
- added R80: 10k, PCM_SparkFun-Resistor:R_0603_1608Metric, F.Cu at (187.2, 138.8)
- C23: value 0.1uF -> 100nF
- U17, U32: footprint Sensor_Distance:ST_VL53L1x -> OptoDevice:ST_VL53L0X
- moved R8 195.6 mm to (48.1, 44.6)
- moved R7 195.0 mm to (48.1, 43.1), turned to 180 degrees
- moved U10 191.8 mm to (52.6, 44.6)
- moved C10 189.5 mm to (48.6, 47.1), turned to -90 degrees
- moved C13 184.9 mm to (60.1, 48.6), turned to 180 degrees
- moved L1 184.6 mm to (65.6, 48.1), turned to -90 degrees
- moved C12 181.8 mm to (60.1, 50.6), turned to 180 degrees
- moved C11 178.8 mm to (60.1, 52.6), turned to 180 degrees
- moved L3 168.3 mm to (263.2, 27.9)
- moved L2 165.2 mm to (56.1, 62.3), turned to 90 degrees
- moved C18 161.8 mm to (62.0, 61.5)
- moved C17 161.1 mm to (62.0, 59.5)
- moved C41 159.9 mm to (256.3, 34.5)
- moved C40 159.9 mm to (256.3, 31.5)
- moved C42 159.9 mm to (256.3, 37.5)
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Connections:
- U2 pad 7: unconnected-(U2-IO8-Pad7) -> /ESP32_GPIO8
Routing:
- net /GND: track 0.00 -> 32.9 mm, vias 0 -> 20
- net /+3V3: track 0.00 -> 25.0 mm, vias 0 -> 2
- net /12V_5V/5V_OUT: track 0.00 -> 21.1 mm, vias 0 -> 3
- net /+12V: track 0.00 -> 10.2 mm, vias 0 -> 11
- net Net-(U10-VFB): track 0.00 -> 3.90 mm
- net Net-(U11-VFB): track 0.00 -> 3.54 mm
- net Net-(U10-VBST): track 0.00 -> 2.93 mm
- net Net-(U11-VBST): track 0.00 -> 2.85 mm
- net Net-(U11-SW): vias 0 -> 10
- net Net-(U10-SW): vias 0 -> 10
- added copper zone on F.Cu, net /+12V
- added copper zone on F.Cu, net /+3V3
- added copper zone on F.Cu, net /12V_5V/5V_OUT
- added copper zone on F.Cu, net /GND
- added copper zone on In1.Cu, net /GND
- added copper zone on F.Cu, net Net-(U10-SW)
- added copper zone on In2.Cu, net Net-(U10-SW)
- added copper zone on F.Cu, net Net-(U11-SW)
- added copper zone on In2.Cu, net Net-(U11-SW)
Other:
- board outline added: 105 x 90 mm
- copper layers 2 -> 4
